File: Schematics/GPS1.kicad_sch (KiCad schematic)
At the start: 1 part, among them J3 Conn_01x05_Pin

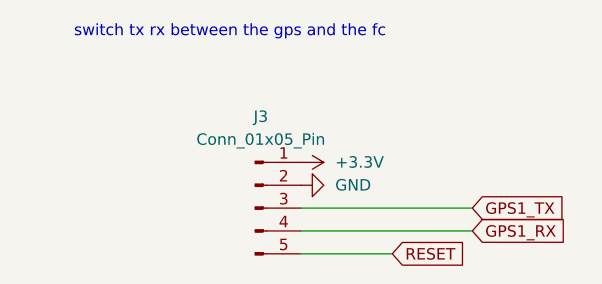
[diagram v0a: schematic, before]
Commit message: finished sensor schematics, added datasheets organized files
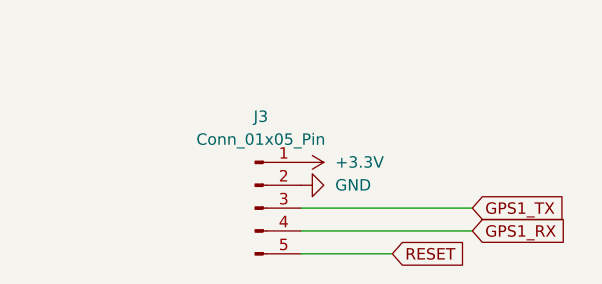
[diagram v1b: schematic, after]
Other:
- note removed: "switch tx rx between the gps and the fc"
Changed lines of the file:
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@@
 	(generator_version "9.0")
 	(paper "A4")
-	(text "switch tx rx between the gps and the fc\n"
-		(exclude_from_sim no)
-		(at 100.076 51.562 0)
-		(effects
-			(font
-				(size 1.27 1.27)
-			)
-		)
-	)
 	(wire
 		(pts

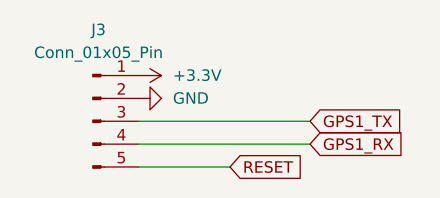
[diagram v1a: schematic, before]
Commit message: added LCSC numbers and footprint values, need to connect schemeatic pins, then can start layout
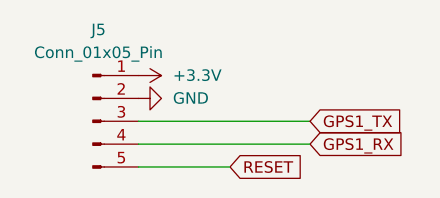
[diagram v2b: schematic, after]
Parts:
- J5: renamed from J3; LCSC Part (none) -> C157991
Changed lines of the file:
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@@
 		(dnp no)
 		(fields_autoplaced yes)
-		(property "Reference" "#PWR013"
+		(property "Reference" "#PWR054"
 			(at 114.3 68.58 0)
 			(effects
@@
 			(project "flightcomputer2"
 				(path "/6cb3dda3-5fe8-4715-b831-354360aa3199/48dec4ea-003d-4181-8fc8-af0c53e2850d"
-					(reference "#PWR013")
+					(reference "#PWR054")
 					(unit 1)
 				)
@@
 		(dnp no)
 		(fields_autoplaced yes)
-		(property "Reference" "J3"
+		(property "Reference" "J5"
 			(at 103.505 60.96 0)
 			(effects
@@
 		)
 		(property "Description" "Generic connector, single row, 01x05, script generated"
+			(at 102.87 71.12 0)
+			(effects
+				(font
+					(size 1.27 1.27)
+				)
+				(hide yes)
+			)
+		)
+		(property "Sim.Device" ""
+			(at 102.87 71.12 0)
+			(effects
+				(font
+					(size 1.27 1.27)
+				)
+				(hide yes)
+			)
+		)
+		(property "Sim.Type" ""
+			(at 102.87 71.12 0)
+			(effects
+				(font
+					(size 1.27 1.27)
+				)
+				(hide yes)
+			)
+		)
+		(property "LCSC Part" "C157991"
 			(at 102.87 71.12 0)
 			(effects
@@
 			(project "flightcomputer2"
 				(path "/6cb3dda3-5fe8-4715-b831-354360aa3199/48dec4ea-003d-4181-8fc8-af0c53e2850d"
-					(reference "J3")
+					(reference "J5")
 					(unit 1)
 				)
@@
 		(dnp no)
 		(fields_autoplaced yes)
-		(property "Reference" "#PWR012"
+		(property "Reference" "#PWR053"
 			(at 104.14 66.04 0)
 			(effects
@@
 			(project "flightcomputer2"
 				(path "/6cb3dda3-5fe8-4715-b831-354360aa3199/48dec4ea-003d-4181-8fc8-af0c53e2850d"
-					(reference "#PWR012")
+					(reference "#PWR053")
 					(unit 1)
 				)

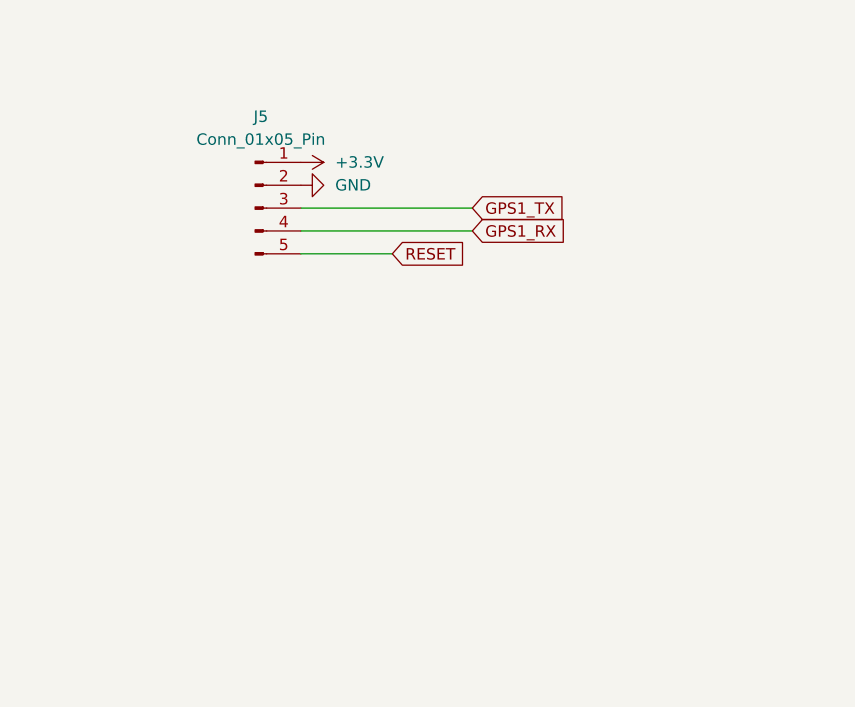
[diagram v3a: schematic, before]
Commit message: fixed symbols and added diodes to power input before ldo
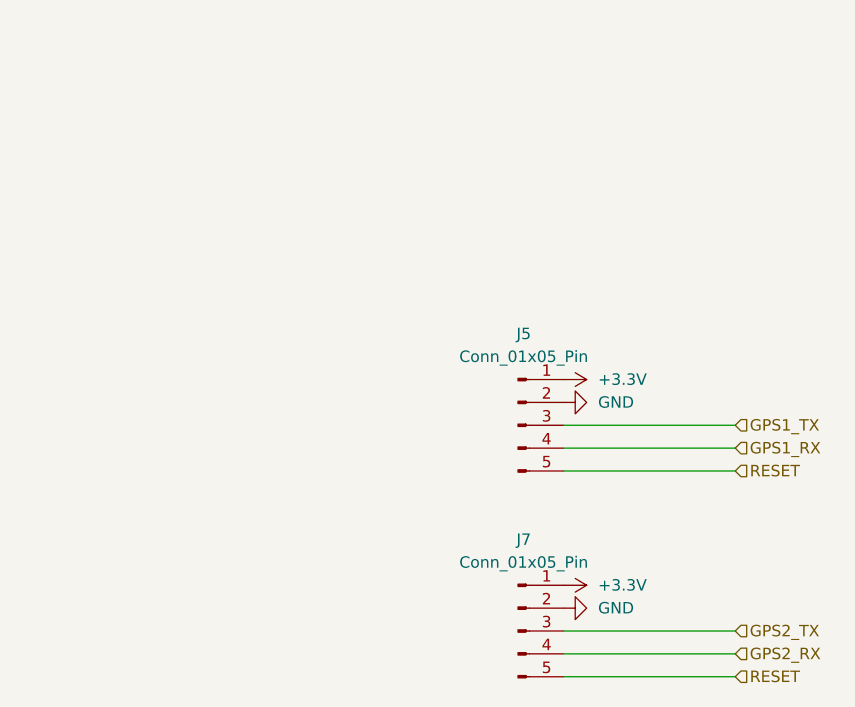
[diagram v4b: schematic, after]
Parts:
- added J7: Conn_01x05_Pin, Library:JST_B5B-XH-A, symbol Connector:Conn_01x05_Pin
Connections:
- net +3.3V: now also J7.1 (Pin_1)
- net GND: now also J7.2 (Pin_2)
- net RESET: now also J7.5 (Pin_5)
- new net GPS2_RX: J7.4 (Pin_4)
- new net GPS2_TX: J7.3 (Pin_3)
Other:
- moved on the sheet: J5

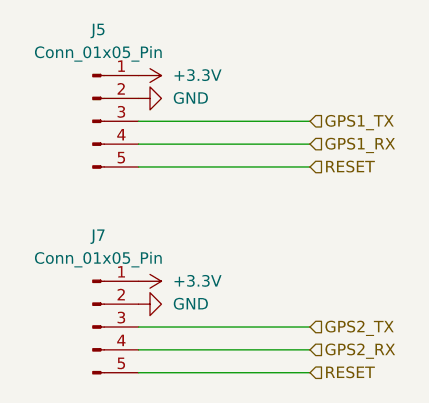
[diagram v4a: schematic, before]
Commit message: added lora correct and organizing sheet pins
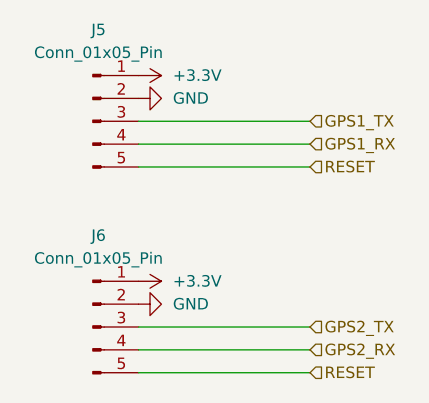
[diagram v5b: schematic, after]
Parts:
- renumbered J7 to J6
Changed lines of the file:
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@@
 		(dnp no)
 		(fields_autoplaced yes)
-		(property "Reference" "#PWR0102"
+		(property "Reference" "#PWR056"
 			(at 133.35 113.03 0)
 			(effects
@@
 			(project "flightcomputer2"
 				(path "/6cb3dda3-5fe8-4715-b831-354360aa3199/48dec4ea-003d-4181-8fc8-af0c53e2850d"
-					(reference "#PWR0102")
+					(reference "#PWR056")
 					(unit 1)
 				)
@@
 		(dnp no)
 		(fields_autoplaced yes)
-		(property "Reference" "#PWR0103"
+		(property "Reference" "#PWR057"
 			(at 143.51 115.57 0)
 			(effects
@@
 			(project "flightcomputer2"
 				(path "/6cb3dda3-5fe8-4715-b831-354360aa3199/48dec4ea-003d-4181-8fc8-af0c53e2850d"
-					(reference "#PWR0103")
+					(reference "#PWR057")
 					(unit 1)
 				)
@@
 		(dnp no)
 		(fields_autoplaced yes)
-		(property "Reference" "#PWR054"
+		(property "Reference" "#PWR055"
 			(at 143.51 92.71 0)
 			(effects
@@
 			(project "flightcomputer2"
 				(path "/6cb3dda3-5fe8-4715-b831-354360aa3199/48dec4ea-003d-4181-8fc8-af0c53e2850d"
-					(reference "#PWR054")
+					(reference "#PWR055")
 					(unit 1)
 				)
@@
 		(dnp no)
 		(fields_autoplaced yes)
-		(property "Reference" "J7"
+		(property "Reference" "J6"
 			(at 132.715 107.95 0)
 			(effects
@@
 			(project "flightcomputer2"
 				(path "/6cb3dda3-5fe8-4715-b831-354360aa3199/48dec4ea-003d-4181-8fc8-af0c53e2850d"
-					(reference "J7")
+					(reference "J6")
 					(unit 1)
 				)
@@
 		(dnp no)
 		(fields_autoplaced yes)
-		(property "Reference" "#PWR053"
+		(property "Reference" "#PWR054"
 			(at 133.35 90.17 0)
 			(effects
@@
 			(project "flightcomputer2"
 				(path "/6cb3dda3-5fe8-4715-b831-354360aa3199/48dec4ea-003d-4181-8fc8-af0c53e2850d"
-					(reference "#PWR053")
-					(unit 1)
-				)
+					(reference "#PWR054")
+					(unit 1)
+				)

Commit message: finished pin assignments and ran ERC all good ready for layout
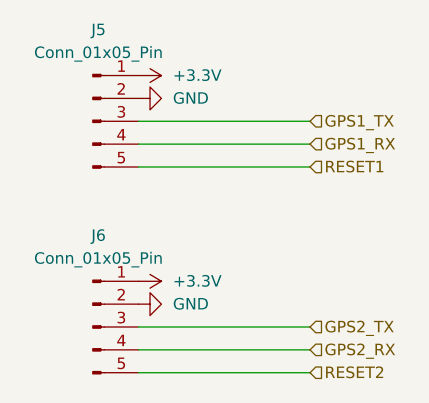
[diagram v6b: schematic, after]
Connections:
- net RESET renamed RESET1
- net RESET1: no longer J6.5 (Pin_5)
- new net RESET2: J6.5 (Pin_5)
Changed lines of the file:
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@@
 		)
 	)
-	(hierarchical_label "RESET"
+	(hierarchical_label "RESET1"
 		(shape input)
 		(at 156.21 100.33 0)
@@
 		)
 	)
-	(hierarchical_label "RESET"
+	(hierarchical_label "RESET2"
 		(shape input)
 		(at 156.21 123.19 0)
@@
 			)
 		)
+		(property "Description_1" ""
+			(at 132.08 95.25 0)
+			(effects
+				(font
+					(size 1.27 1.27)
+				)
+				(hide yes)
+			)
+		)
+		(property "MF" ""
+			(at 132.08 95.25 0)
+			(effects
+				(font
+					(size 1.27 1.27)
+				)
+				(hide yes)
+			)
+		)
+		(property "MP" ""
+			(at 132.08 95.25 0)
+			(effects
+				(font
+					(size 1.27 1.27)
+				)
+				(hide yes)
+			)
+		)
+		(property "Package" ""
+			(at 132.08 95.25 0)
+			(effects
+				(font
+					(size 1.27 1.27)
+				)
+				(hide yes)
+			)
+		)
+		(property "Price" ""
+			(at 132.08 95.25 0)
+			(effects
+				(font
+					(size 1.27 1.27)
+				)
+				(hide yes)
+			)
+		)
+		(property "Purchase-URL" ""
+			(at 132.08 95.25 0)
+			(effects
+				(font
+					(size 1.27 1.27)
+				)
+				(hide yes)
+			)
+		)
 		(pin "2"
 		)
@@
 			(at 132.08 118.11 0)
 			(effects
+				(font
+					(size 1.27 1.27)
+				)
+				(hide yes)
+			)
+		)
+		(property "Description_1" ""
+			(at 132.08 118.11 0)
+			(effects
+				(font
+					(size 1.27 1.27)
+				)
+				(hide yes)
+			)
+		)
+		(property "MF" ""
+			(at 132.08 118.11 0)
+			(effects
+				(font
+					(size 1.27 1.27)
+				)
+				(hide yes)
+			)
+		)
+		(property "MP" ""
+			(at 132.08 118.11 0)
+			(effects
+				(font
+					(size 1.27 1.27)
+				)
+				(hide yes)
+			)
+		)
+		(property "Package" ""
+			(at 132.08 118.11 0)
+			(effects
+				(font
+					(size 1.27 1.27)
+				)
+				(hide yes)
+			)
+		)
+		(property "Price" ""
+			(at 132.08 118.11 0)
+			(effects
+				(font
+					(size 1.27 1.27)
+				)
+				(hide yes)
+			)
+		)
+		(property "Purchase-URL" ""
+			(at 132.08 118.11 0)
+			(effects
